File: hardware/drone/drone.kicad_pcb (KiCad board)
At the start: 2 copper layers, 25 parts, among them J1 54548-2272, J2 BM08B-SRSS-TB_LF__SN_, J4 Conn_ARM_SWD_TagConnect_TC2030, Q1 ISP650P06NM, U1 STM32N645I0, U10 PE4259, U11 TAC5111IRGER, U2 SX1262IMLTRT, U20 TVS0500DRV, U22 LIS2MDL, U3 TPS628303, U4 TPS7A2118PQWDSGRQ1, U5 TPS628303, U6 MX25UW25645GXDI00, U7 CC3350, U8 DPX167125DT-8197B1, U9 DEA162450BT-1295A1

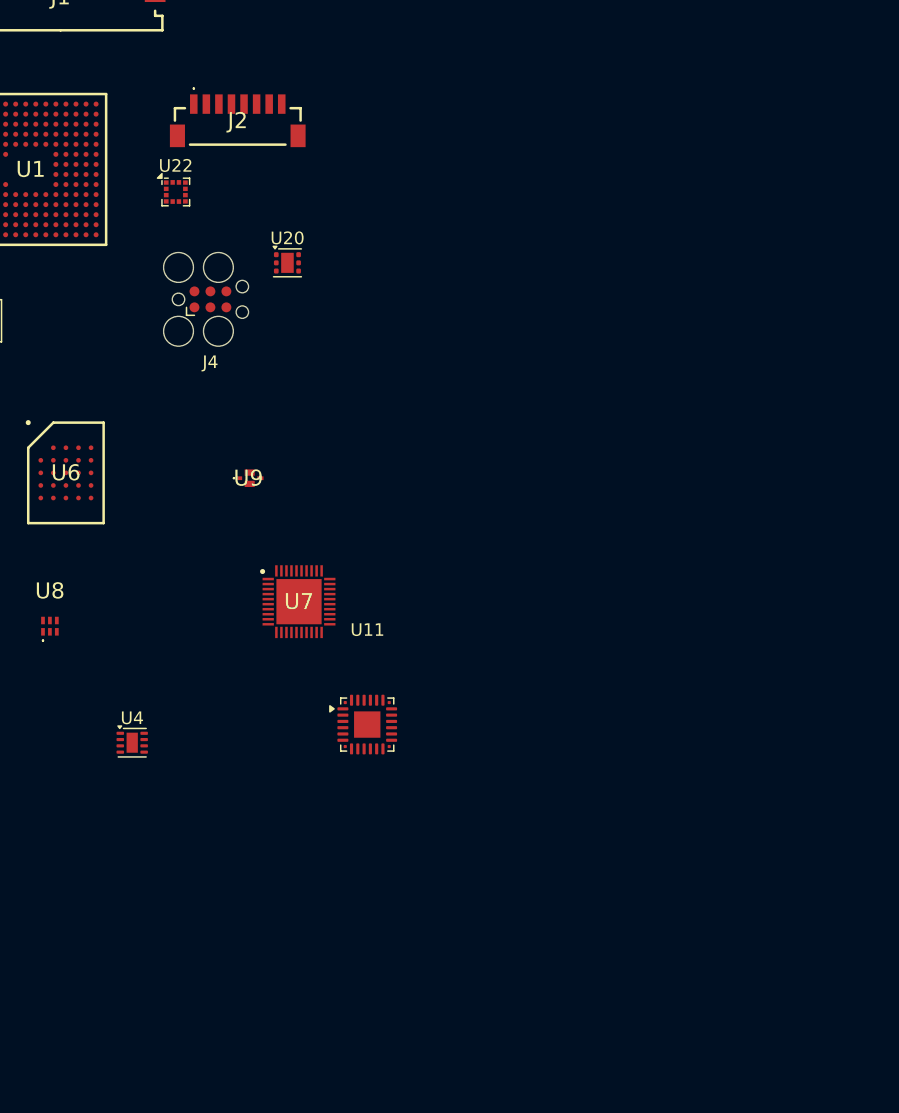
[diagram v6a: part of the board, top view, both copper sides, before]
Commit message: Continued footprint assignments
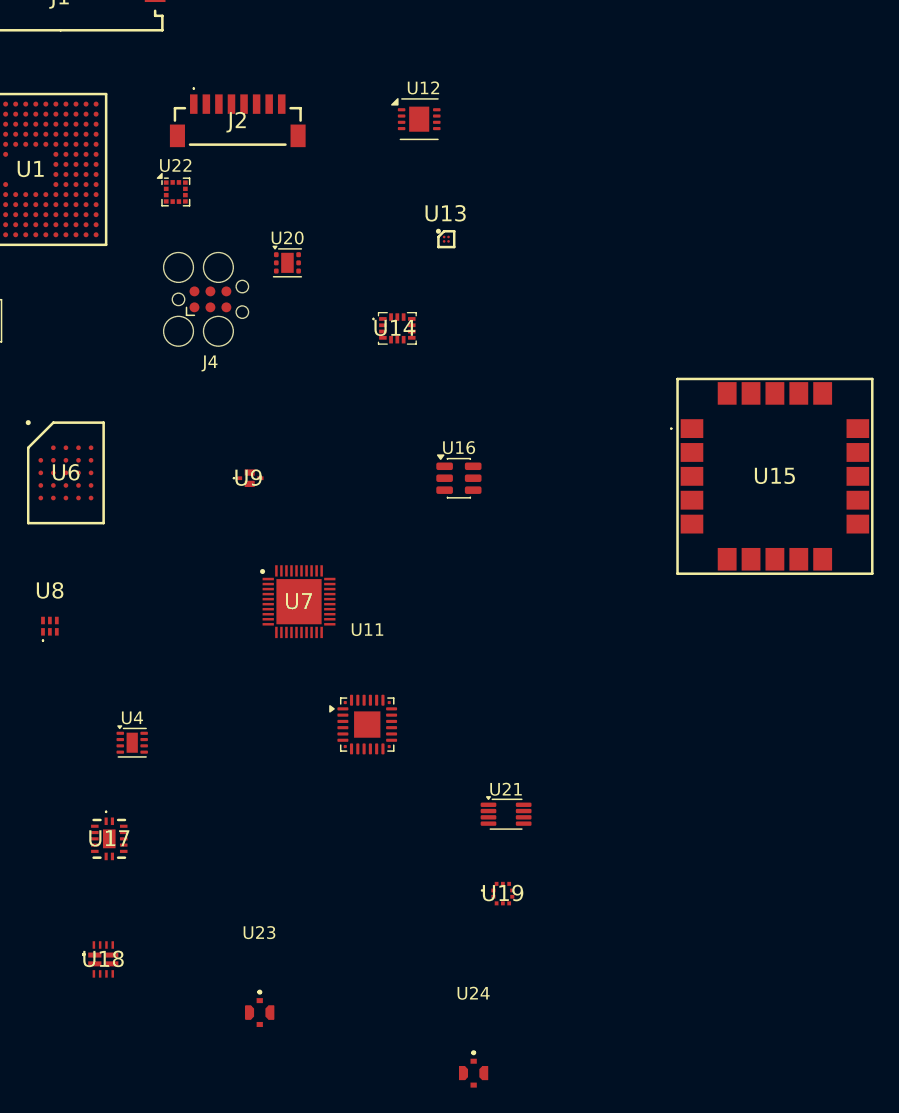
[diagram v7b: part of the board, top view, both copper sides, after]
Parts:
- added U12: LM4670SD/NOPB, Package_SON:WSON-8-1EP_3x3mm_P0.5mm_EP1.6x2.0mm, F.Cu at (90.9, 62.9)
- added U13: LP5907, LP5907A28YKMR:BGA4C35P2X2_64X64X50, F.Cu at (93.1, 72.5)
- added U14: ICM-42688-P, ICM-42688-P:IIM42352, F.Cu at (89.2, 79.6)
- added U15: SAM_M10Q, SAM-M10Q:SAMM10Q, F.Cu at (119.2, 91.3)
- added U16: LMR51635XFDDCR, Package_TO_SOT_SMD:SOT-23-6, F.Cu at (94.1, 91.5)
- added U17: TXU0204, TXU0204BQAR:TXU0204BQAR, F.Cu at (66.3, 120.2)
- added U18: TPS2121, TPS2121RUXT:TPS2121RUXT, F.Cu at (65.8, 129.8)
- added U19: BMP581, BMP581:BMP581, F.Cu at (97.6, 124.6)
- added U21: TCA9406DC, Package_SO:VSSOP-8_2.3x2mm_P0.5mm, F.Cu at (97.9, 118.2)
- added U23: MM8030_2610RJ3, SoftDroneLibrary:MM8030-2610RJ3, F.Cu at (78.2, 134.0)
- added U24: MM8030_2610RJ3, SoftDroneLibrary:MM8030-2610RJ3, F.Cu at (95.3, 138.8)
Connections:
- U1 pad E10: GNSS_TIMEPULSE -> GNSS_TIM_1V8

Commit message: More footprints
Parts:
- added C11: 100n, Capacitor_SMD:C_0201_0603Metric, F.Cu at (121.0, 125.8)
- added C119: 100n, Capacitor_SMD:C_0201_0603Metric, F.Cu at (132.6, 157.8)
- added C12: 100n, Capacitor_SMD:C_0201_0603Metric, F.Cu at (121.0, 127.5)
- added C120: 10u, Capacitor_SMD:CP_Elec_4x5.4, F.Cu at (142.6, 151.8)
- added C121: 100n, Capacitor_SMD:C_0201_0603Metric, F.Cu at (132.6, 159.6)
- added C123: 100n, Capacitor_SMD:C_0201_0603Metric, F.Cu at (121.3, 155.9)
- added C124: 1u, Capacitor_SMD:C_0402_1005Metric, F.Cu at (121.5, 154.1)
- added C16: 100n, Capacitor_SMD:C_0201_0603Metric, F.Cu at (121.0, 129.3)
- added C19: 100n, Capacitor_SMD:C_0201_0603Metric, F.Cu at (121.0, 131.1)
- added C20: 100n, Capacitor_SMD:C_0201_0603Metric, F.Cu at (121.0, 132.8)
- added C22: 100n, Capacitor_SMD:C_0201_0603Metric, F.Cu at (121.0, 134.6)
- added C23: 100n, Capacitor_SMD:C_0201_0603Metric, F.Cu at (121.0, 136.3)
- added C25: 100n, Capacitor_SMD:C_0201_0603Metric, F.Cu at (121.0, 138.1)
- added C32: 100n, Capacitor_SMD:C_0402_1005Metric, F.Cu at (133.0, 137.8)
- added C33: 100n, Capacitor_SMD:C_0402_1005Metric, F.Cu at (133.0, 139.7)
- added C34: 100n, Capacitor_SMD:C_0402_1005Metric, F.Cu at (133.0, 141.7)
- added C35: 100n, Capacitor_SMD:C_0201_0603Metric, F.Cu at (125.5, 125.8)
- added C36: 100n, Capacitor_SMD:C_0201_0603Metric, F.Cu at (125.5, 127.5)
- added C37: 100n, Capacitor_SMD:C_0201_0603Metric, F.Cu at (125.5, 129.3)
- added C38: 100n, Capacitor_SMD:C_0201_0603Metric, F.Cu at (125.5, 131.1)
- added C39: 100n, Capacitor_SMD:C_0201_0603Metric, F.Cu at (125.5, 132.8)
- added C40: 1u, Capacitor_SMD:C_0201_0603Metric, F.Cu at (125.5, 134.6)
- added C41: 1u, Capacitor_SMD:C_0201_0603Metric, F.Cu at (125.5, 136.3)
- added C42: 1u, Capacitor_SMD:C_0402_1005Metric, F.Cu at (128.1, 125.9)
- added C46: 47p, Capacitor_SMD:C_0402_1005Metric, F.Cu at (133.0, 125.9)
- added C47: 47n, Capacitor_SMD:C_0402_1005Metric, F.Cu at (133.0, 127.9)
- added C48: 3p, Capacitor_SMD:C_0402_1005Metric, F.Cu at (133.0, 129.8)
- added C49: 100n, Capacitor_SMD:C_0402_1005Metric, F.Cu at (116.6, 154.1)
- added C50: 5.6p, Capacitor_SMD:C_0402_1005Metric, F.Cu at (133.0, 131.8)
- added C51: 39p, Capacitor_SMD:C_0402_1005Metric, F.Cu at (133.0, 133.8)
- added C52: 1.8p, Capacitor_SMD:C_0402_1005Metric, F.Cu at (135.8, 125.9)
- added C53: 1.8p, Capacitor_SMD:C_0402_1005Metric, F.Cu at (135.8, 127.9)
- added C54: 2.4p, Capacitor_SMD:C_0402_1005Metric, F.Cu at (135.8, 129.8)
- added C55: 100n, Capacitor_SMD:C_0402_1005Metric, F.Cu at (116.6, 156.0)
- added C56: 470n, Capacitor_SMD:C_0402_1005Metric, F.Cu at (135.8, 131.8)
- added C57: 1u, Capacitor_SMD:C_0402_1005Metric, F.Cu at (135.8, 133.8)
- added C61: 1n, Capacitor_SMD:C_0402_1005Metric, F.Cu at (138.7, 125.9)
- added C64: 100n, Capacitor_SMD:C_0402_1005Metric, F.Cu at (138.7, 127.9)
- added C65: 100n, Capacitor_SMD:C_0402_1005Metric, F.Cu at (138.7, 129.8)
- added C82: 100n, Capacitor_SMD:C_0201_0603Metric, F.Cu at (132.6, 150.8)
- added C83: 2.2u, Capacitor_SMD:C_0402_1005Metric, F.Cu at (135.3, 156.8)
- added C84: 10n, Capacitor_SMD:C_0201_0603Metric, F.Cu at (132.6, 152.6)
- added C90: 100n, Capacitor_SMD:C_0201_0603Metric, F.Cu at (132.6, 154.3)
- added C91: 100n, Capacitor_SMD:C_0201_0603Metric, F.Cu at (132.6, 156.1)
- added U25: ECMF2-40A100N6, ECMF2-40A100N6:ECMF240A100N6, F.Cu at (110.4, 110.6)
- added U26: ECMF2-40A100N6, ECMF2-40A100N6:ECMF240A100N6, F.Cu at (114.9, 110.6)
- added U27: ECMF2-40A100N6, ECMF2-40A100N6:ECMF240A100N6, F.Cu at (119.4, 110.6)
- U10: footprint PE4259-63:SOT65P210X110-6N -> SoftDroneLibrary:PE4259
- moved U10 3.55 mm to (45.8, 103.9)
